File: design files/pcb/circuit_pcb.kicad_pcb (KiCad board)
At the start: 2 copper layers, 58.4 x 108.7 mm, 69 parts, among them J1 TRIG1_IN, J10 CVS1, J11 CVR1, J12 CVS2, J13 CVR2, J2 TRIG2_IN, J3 CVA1, J4 OUT_1, J5 MCP4728, J6 CVA2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

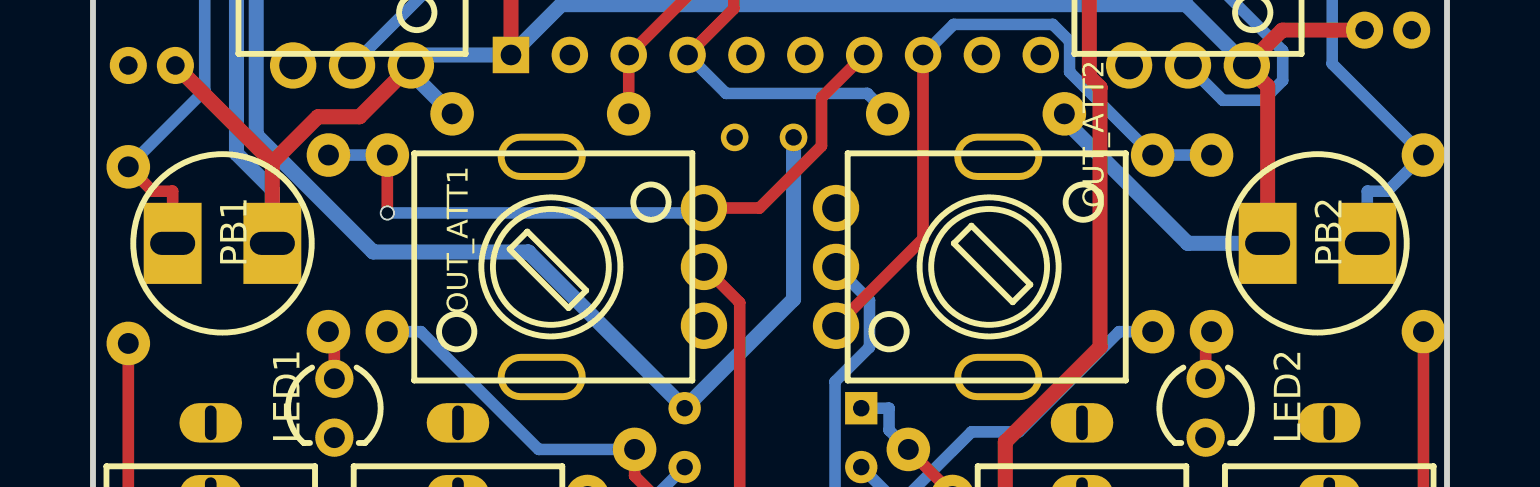
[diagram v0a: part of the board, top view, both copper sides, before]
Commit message: V1.1 pcb (only changes are bigger switch holes and a nametag)
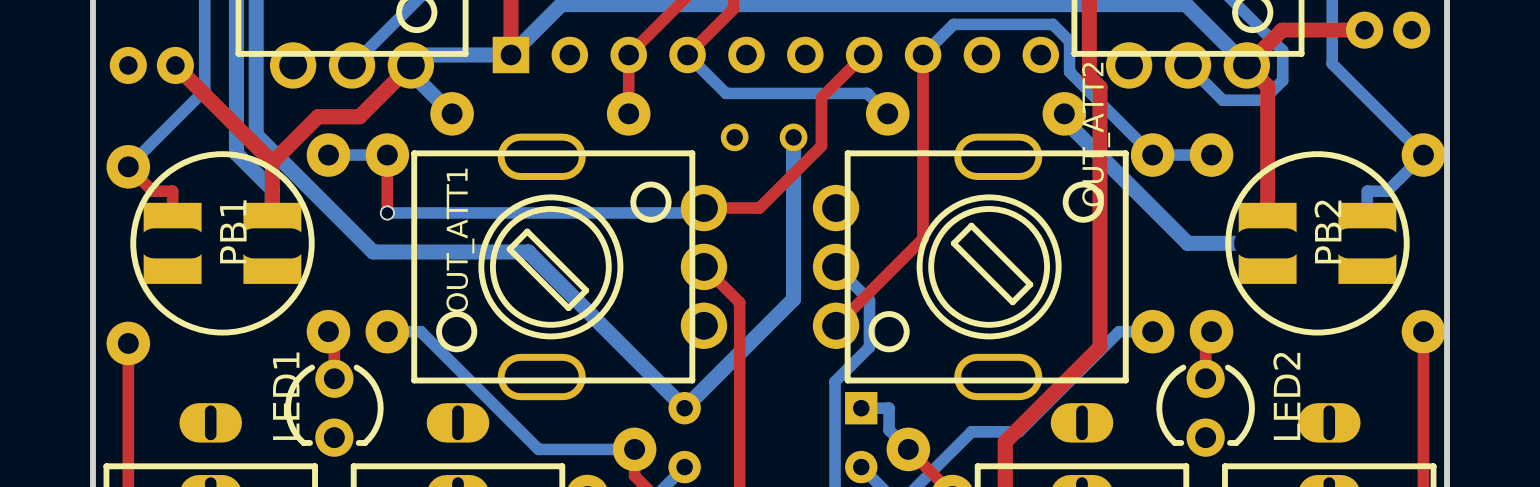
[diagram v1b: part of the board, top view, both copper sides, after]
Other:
- board text added: "CIrcuit and PCB by Patrick V."
- board text added: "Testbild Dual VCADSR v1.1"
